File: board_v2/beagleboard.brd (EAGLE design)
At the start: 69.8 x 54.6 mm, 26 parts, among them U1 DWM1000, X1 5566-2, X2 04-JST-B4B-XH-A

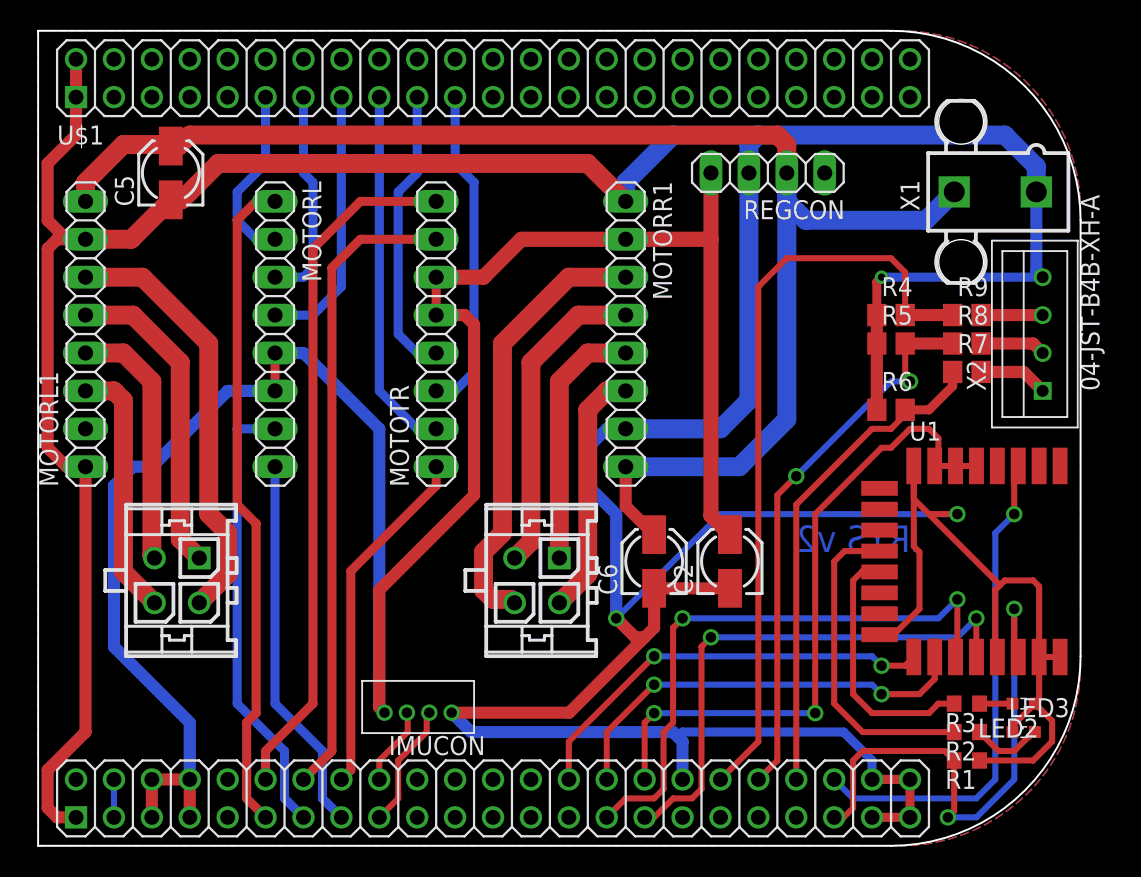
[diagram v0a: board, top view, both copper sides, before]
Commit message: added distance sensor connectors
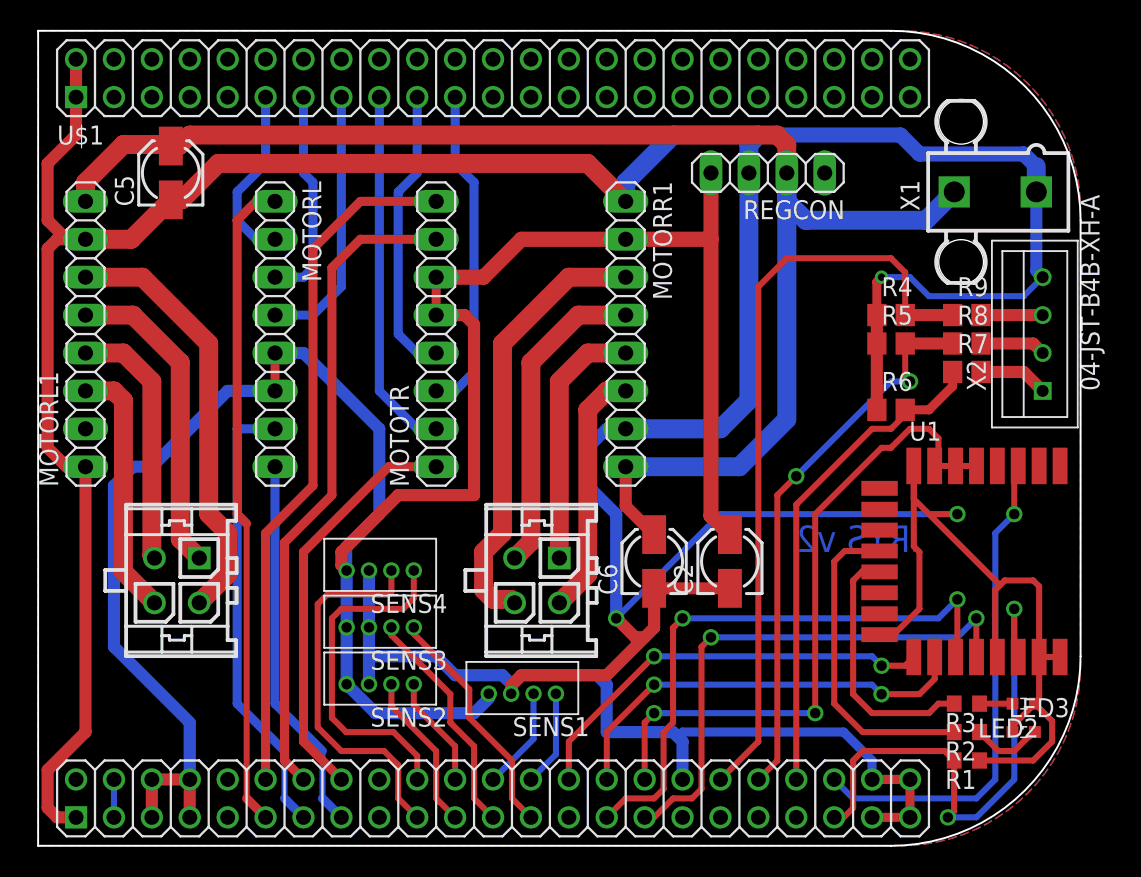
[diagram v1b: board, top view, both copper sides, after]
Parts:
- removed IMUCON: B4B-ZR, jst:B4B-ZR
- added SENS1, SENS2, SENS3, SENS4: B4B-ZR, jst:B4B-ZR
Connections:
- removed net N$100: U$1.71
- removed net N$74: U$1.66
- removed net N$75: U$1.68
- removed net N$76: U$1.70
- removed net N$77: U$1.72
- removed net N$97: U$1.65
- removed net N$98: U$1.67
- removed net N$99: U$1.69
- new net D1ECHO: SENS1.3, U$1.70
- new net D1TRIG: SENS1.4, U$1.72
- new net D2ECHO: SENS2.3, U$1.67
- new net D2TRIG: SENS2.4, U$1.68
- new net D3ECHO: SENS3.3, U$1.69
- new net D3TRIG: SENS3.4, U$1.71
- new net D4ECHO: SENS4.3, U$1.65
- new net D4TRIG: SENS4.4, U$1.66
- net +5V: now also SENS1.1, SENS2.1, SENS3.1, SENS4.1; no longer IMUCON.1
- net GND: now also SENS1.2, SENS2.2, SENS3.2, SENS4.2; no longer IMUCON.4
- net SCL1: no longer IMUCON.3
- net SDA1: no longer IMUCON.2
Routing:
- net D4ECHO: track 0.00 -> 25.4 mm
- net D4TRIG: track 0.00 -> 22.9 mm
- net D3TRIG: track 0.00 -> 16.0 mm
- net D3ECHO: track 0.00 -> 15.6 mm
- net GND: track 356.7 -> 371.9 mm
- net D2ECHO: track 0.00 -> 10.7 mm
- net SCL1: track 8.40 -> 0.00 mm
- net D2TRIG: track 0.00 -> 7.53 mm
- net D1ECHO: track 0.00 -> 6.87 mm
- net D1TRIG: track 0.00 -> 6.44 mm
- net SDA1: track 5.29 -> 0.00 mm
- net +5V: track 152.0 -> 156.4 mm
- net MREN: track 23.6 -> 27.5 mm
- net MRSTEP: track 42.9 -> 43.9 mm
- net MLEN: track 44.4 -> 43.9 mm

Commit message: gerbers
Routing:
- net +5V: track 156.4 -> 157.0 mm
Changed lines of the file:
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@@
 <board>
 <plain>
-<text x="61.595" y="20.32" size="1.778" layer="16" rot="MR0">iRYS v2</text>
+<text x="61.2775" y="19.685" size="1.778" layer="16" rot="MR0">iRYS v2</text>
 </plain>
 <attributes>
@@
 <wire x1="58.74" y1="29.845" x2="58.74" y2="38.42" width="0.6096" layer="1"/>
 <wire x1="58.74" y1="38.42" x2="59.055" y2="38.735" width="0.6096" layer="1"/>
-<via x="59.055" y="38.735" extent="1-16" drill="0.5" shape="octagon"/>
+<via x="59.055" y="38.735" extent="1-16" drill="0.5"/>
 <wire x1="43.18" y1="14.605" x2="42.545" y2="14.605" width="0.8128" layer="1"/>
 <wire x1="42.545" y1="14.605" x2="41.275" y2="15.875" width="0.8128" layer="1"/>
@@
 <wire x1="32.735" y1="10.825" x2="32.735" y2="10.51" width="0.8128" layer="16"/>
 <wire x1="32.735" y1="10.51" x2="31.75" y2="9.525" width="0.8128" layer="16"/>
-<wire x1="31.75" y1="9.525" x2="25.145" y2="9.525" width="0.8128" layer="16"/>
-<wire x1="25.145" y1="9.525" x2="23.21" y2="11.46" width="0.8128" layer="16"/>
+<wire x1="31.75" y1="9.525" x2="24.1925" y2="9.525" width="0.8128" layer="16"/>
 <wire x1="23.21" y1="19.08" x2="23.21" y2="15.27" width="0.8128" layer="16"/>
 <wire x1="23.21" y1="15.27" x2="23.21" y2="11.46" width="0.8128" layer="16"/>
+<wire x1="23.21" y1="11.46" x2="23.21" y2="10.5075" width="0.8128" layer="16"/>
+<wire x1="23.21" y1="10.5075" x2="24.1925" y2="9.525" width="0.8128" layer="16"/>
 </signal>
 <signal name="CSN">

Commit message: gpioadjustment
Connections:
- removed net N$105: U$1.81
- removed net N$106: U$1.83
- removed net N$107: U$1.85
- removed net N$45: U$1.7
- removed net N$46: U$1.9
- removed net N$69: U$1.56
- removed net N$92: U$1.55
- new net N$17: U$1.19
- new net N$19: U$1.21
- net +3V3: no longer U$1.78
- net D3TRIG: now also U$1.81; no longer U$1.71
- net D4ECHO: now also U$1.85; no longer U$1.65
- net D4TRIG: now also U$1.83; no longer U$1.66
- net MLM0: now also U$1.7; no longer U$1.11
- net MLM1: now also U$1.9; no longer U$1.13
- net MLM2: now also U$1.11; no longer U$1.15
- net MRM0: now also U$1.13; no longer U$1.17
- net MRM1: now also U$1.15; no longer U$1.21
- net MRM2: now also U$1.17; no longer U$1.19
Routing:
- net MRM0: track 24.5 -> 4.86 mm
- net MLM2: track 17.9 -> 5.23 mm
- net MLM1: track 14.5 -> 9.42 mm
- net MRM2: track 19.5 -> 14.4 mm
- net MLM0: track 12.1 -> 7.67 mm
- net MRM1: track 22.0 -> 17.6 mm
- net +3V3: track 44.5 -> 40.7 mm
- net D3TRIG: track 16.0 -> 14.2 mm
- net D4ECHO: track 25.4 -> 23.6 mm
- net D4TRIG: track 22.9 -> 21.3 mm
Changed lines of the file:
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@@
 <?xml version="1.0" encoding="utf-8"?>
 <!DOCTYPE eagle SYSTEM "eagle.dtd">
-<eagle version="7.1.0">
+<eagle version="7.7.0">
 <drawing>
 <settings>
@@
 <wire x1="65.415" y1="26.085" x2="64.015" y2="26.085" width="0.4064" layer="1"/>
 <wire x1="64.015" y1="26.085" x2="62.615" y2="26.085" width="0.4064" layer="1"/>
-<contactref element="U$1" pad="78"/>
-<wire x1="43.18" y1="5.08" x2="43.18" y2="8.89" width="0.4064" layer="1"/>
 <wire x1="43.18" y1="8.89" x2="43.815" y2="9.525" width="0.4064" layer="1"/>
 <via x="43.815" y="9.525" extent="1-16" drill="0.7"/>
@@
 <signal name="MRM0">
 <contactref element="MOTOTR" pad="2"/>
-<contactref element="U$1" pad="17"/>
-<wire x1="25.4" y1="50.8" x2="25.4" y2="31.115" width="0.6096" layer="16"/>
 <wire x1="25.4" y1="31.115" x2="27.94" y2="28.575" width="0.6096" layer="16"/>
 <wire x1="27.94" y1="28.575" x2="29.21" y2="28.575" width="0.6096" layer="16"/>
+<contactref element="U$1" pad="13"/>
+<wire x1="25.4" y1="31.115" x2="20.32" y2="50.8" width="0" layer="19" extent="16-16"/>
 </signal>
 <signal name="MRM1">
 <contactref element="MOTOTR" pad="3"/>
-<contactref element="U$1" pad="21"/>
-<wire x1="30.48" y1="50.8" x2="30.48" y2="46.355" width="0.6096" layer="16"/>
 <wire x1="30.48" y1="46.355" x2="31.75" y2="45.085" width="0.6096" layer="16"/>
 <wire x1="31.75" y1="45.085" x2="31.75" y2="32.385" width="0.6096" layer="16"/>
 <wire x1="31.75" y1="32.385" x2="30.48" y2="31.115" width="0.6096" layer="16"/>
 <wire x1="30.48" y1="31.115" x2="29.21" y2="31.115" width="0.6096" layer="16"/>
+<contactref element="U$1" pad="15"/>
+<wire x1="30.48" y1="46.355" x2="22.86" y2="50.8" width="0" layer="19" extent="16-16"/>
 </signal>
 <signal name="MRM2">
 <contactref element="MOTOTR" pad="4"/>
-<contactref element="U$1" pad="19"/>
-<wire x1="27.94" y1="50.8" x2="27.94" y2="45.72" width="0.6096" layer="16"/>
 <wire x1="27.94" y1="45.72" x2="26.67" y2="44.45" width="0.6096" layer="16"/>
 <wire x1="26.67" y1="44.45" x2="26.67" y2="34.925" width="0.6096" layer="16"/>
 <wire x1="26.67" y1="34.925" x2="27.94" y2="33.655" width="0.6096" layer="16"/>
 <wire x1="27.94" y1="33.655" x2="29.21" y2="33.655" width="0.6096" layer="16"/>
+<contactref element="U$1" pad="17"/>
+<wire x1="27.94" y1="45.72" x2="25.4" y2="50.8" width="0" layer="19" extent="16-16"/>
 </signal>
 <signal name="MLM0">
 <contactref element="MOTORL" pad="2"/>
-<contactref element="U$1" pad="11"/>
-<wire x1="17.78" y1="50.8" x2="17.78" y2="46.355" width="0.6096" layer="16"/>
 <wire x1="17.78" y1="46.355" x2="15.875" y2="44.45" width="0.6096" layer="16"/>
 <wire x1="15.875" y1="44.45" x2="15.875" y2="42.545" width="0.6096" layer="16"/>
 <wire x1="15.875" y1="42.545" x2="17.145" y2="41.275" width="0.6096" layer="16"/>
 <wire x1="17.145" y1="41.275" x2="18.415" y2="41.275" width="0.6096" layer="16"/>
+<contactref element="U$1" pad="7"/>
+<wire x1="17.78" y1="46.355" x2="12.7" y2="50.8" width="0" layer="19" extent="16-16"/>
 </signal>
 <signal name="MLM1">
 <contactref element="MOTORL" pad="3"/>
-<contactref element="U$1" pad="13"/>
-<wire x1="20.32" y1="50.8" x2="20.32" y2="45.72" width="0.6096" layer="16"/>
 <wire x1="20.32" y1="45.72" x2="20.955" y2="45.085" width="0.6096" layer="16"/>
 <wire x1="20.955" y1="45.085" x2="20.955" y2="39.37" width="0.6096" layer="16"/>
 <wire x1="20.955" y1="39.37" x2="20.32" y2="38.735" width="0.6096" layer="16"/>
 <wire x1="20.32" y1="38.735" x2="18.415" y2="38.735" width="0.6096" layer="16"/>
+<contactref element="U$1" pad="9"/>
+<wire x1="20.32" y1="45.72" x2="15.24" y2="50.8" width="0" layer="19" extent="16-16"/>
 </signal>
 <signal name="MLM2">
 <contactref element="MOTORL" pad="4"/>
-<contactref element="U$1" pad="15"/>
-<wire x1="22.86" y1="50.8" x2="22.86" y2="38.1" width="0.6096" layer="16"/>
 <wire x1="22.86" y1="38.1" x2="20.955" y2="36.195" width="0.6096" layer="16"/>
 <wire x1="20.955" y1="36.195" x2="18.415" y2="36.195" width="0.6096" layer="16"/>
+<contactref element="U$1" pad="11"/>
+<wire x1="22.86" y1="38.1" x2="17.78" y2="50.8" width="0" layer="19" extent="16-16"/>
 </signal>
 <signal name="N$18">
@@
 <contactref element="U$1" pad="5"/>
 </signal>
-<signal name="N$45">
-<contactref element="U$1" pad="7"/>
-</signal>
-<signal name="N$46">
-<contactref element="U$1" pad="9"/>
-</signal>
 <signal name="N$53">
 <contactref element="U$1" pad="23"/>
@@
 <contactref element="U$1" pad="45"/>
 </signal>
-<signal name="N$69">
-<contactref element="U$1" pad="56"/>
-</signal>
 <signal name="D4TRIG">
-<contactref element="U$1" pad="66"/>
 <contactref element="SENS4" pad="4"/>
 <wire x1="27.71" y1="19.08" x2="27.71" y2="17.2325" width="0.4064" layer="1"/>
@@
 <wire x1="22.86" y1="16.51" x2="22.225" y2="15.875" width="0.4064" layer="1"/>
 <wire x1="22.225" y1="15.875" x2="22.225" y2="9.2075" width="0.4064" layer="1"/>
-<wire x1="27.94" y1="5.08" x2="27.94" y2="6.6675" width="0.4064" layer="1"/>
 <wire x1="27.94" y1="6.6675" x2="26.3525" y2="8.255" width="0.4064" layer="1"/>
 <wire x1="26.3525" y1="8.255" x2="23.1775" y2="8.255" width="0.4064" layer="1"/>
 <wire x1="23.1775" y1="8.255" x2="22.225" y2="9.2075" width="0.4064" layer="1"/>
+<contactref element="U$1" pad="83"/>
+<wire x1="27.94" y1="6.6675" x2="50.8" y2="2.54" width="0" layer="19" extent="1-1"/>
 </signal>
 <signal name="D2TRIG">
@@
 <wire x1="37.235" y1="6.755" x2="35.56" y2="5.08" width="0.4064" layer="16"/>
 </signal>
-<signal name="N$92">
-<contactref element="U$1" pad="55"/>
-</signal>
 <signal name="D4ECHO">
-<contactref element="U$1" pad="65"/>
 <contactref element="SENS4" pad="3"/>
 <wire x1="26.21" y1="19.08" x2="26.21" y2="17.6375" width="0.4064" layer="1"/>
@@
 <wire x1="25.7175" y1="6.985" x2="26.67" y2="6.0325" width="0.4064" layer="1"/>
 <wire x1="26.67" y1="6.0325" x2="26.67" y2="3.81" width="0.4064" layer="1"/>
-<wire x1="26.67" y1="3.81" x2="27.94" y2="2.54" width="0.4064" layer="1"/>
+<contactref element="U$1" pad="85"/>
+<wire x1="26.67" y1="3.81" x2="53.34" y2="2.54" width="0" layer="19" extent="1-1"/>
 </signal>
 <signal name="D2ECHO">
@@
 <signal name="D3TRIG">
 <contactref element="SENS3" pad="4"/>
-<contactref element="U$1" pad="71"/>
 <wire x1="27.71" y1="15.27" x2="27.71" y2="14.835" width="0.4064" layer="1"/>
 <wire x1="27.71" y1="14.835" x2="31.4325" y2="11.1125" width="0.4064" layer="1"/>
@@
 <wire x1="31.4325" y1="9.2075" x2="34.29" y2="6.35" width="0.4064" layer="1"/>
 <wire x1="34.29" y1="6.35" x2="34.29" y2="3.81" width="0.4064" layer="1"/>
-<wire x1="34.29" y1="3.81" x2="35.56" y2="2.54" width="0.4064" layer="1"/>
+<contactref element="U$1" pad="81"/>
+<wire x1="34.29" y1="3.81" x2="48.26" y2="2.54" width="0" layer="19" extent="1-1"/>
 </signal>
 <signal name="D3ECHO">
@@
 <signal name="N$104">
 <contactref element="U$1" pad="79"/>
-</signal>
-<signal name="N$105">
-<contactref element="U$1" pad="81"/>
-</signal>
-<signal name="N$106">
-<contactref element="U$1" pad="83"/>
-</signal>
-<signal name="N$107">
-<contactref element="U$1" pad="85"/>
 </signal>
 <signal name="N$16">
@@
 <wire x1="7.62" y1="5.08" x2="7.62" y2="2.54" width="0.4064" layer="16"/>
 </signal>
+<signal name="N$17">
+<contactref element="U$1" pad="19"/>
+</signal>
+<signal name="N$19">
+<contactref element="U$1" pad="21"/>
+</signal>
 </signals>

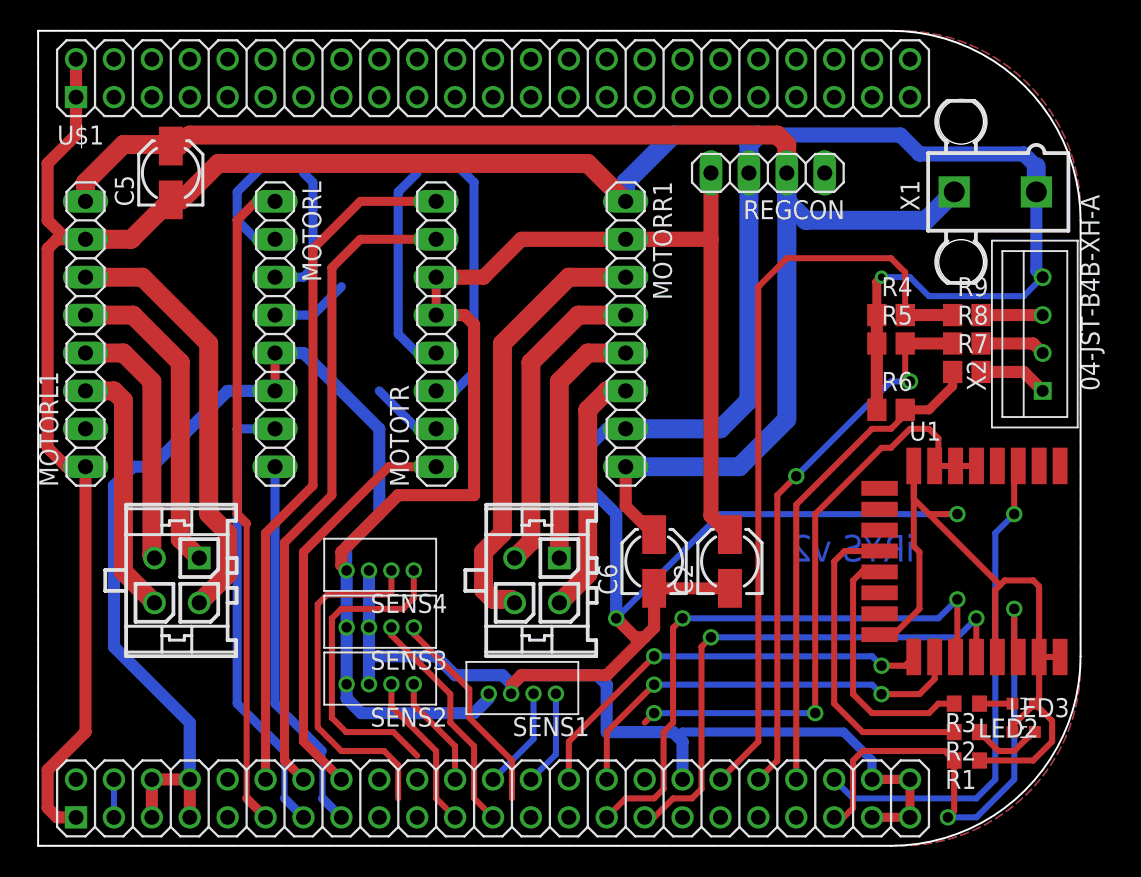
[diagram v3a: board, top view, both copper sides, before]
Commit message: check and reconfigure gpios
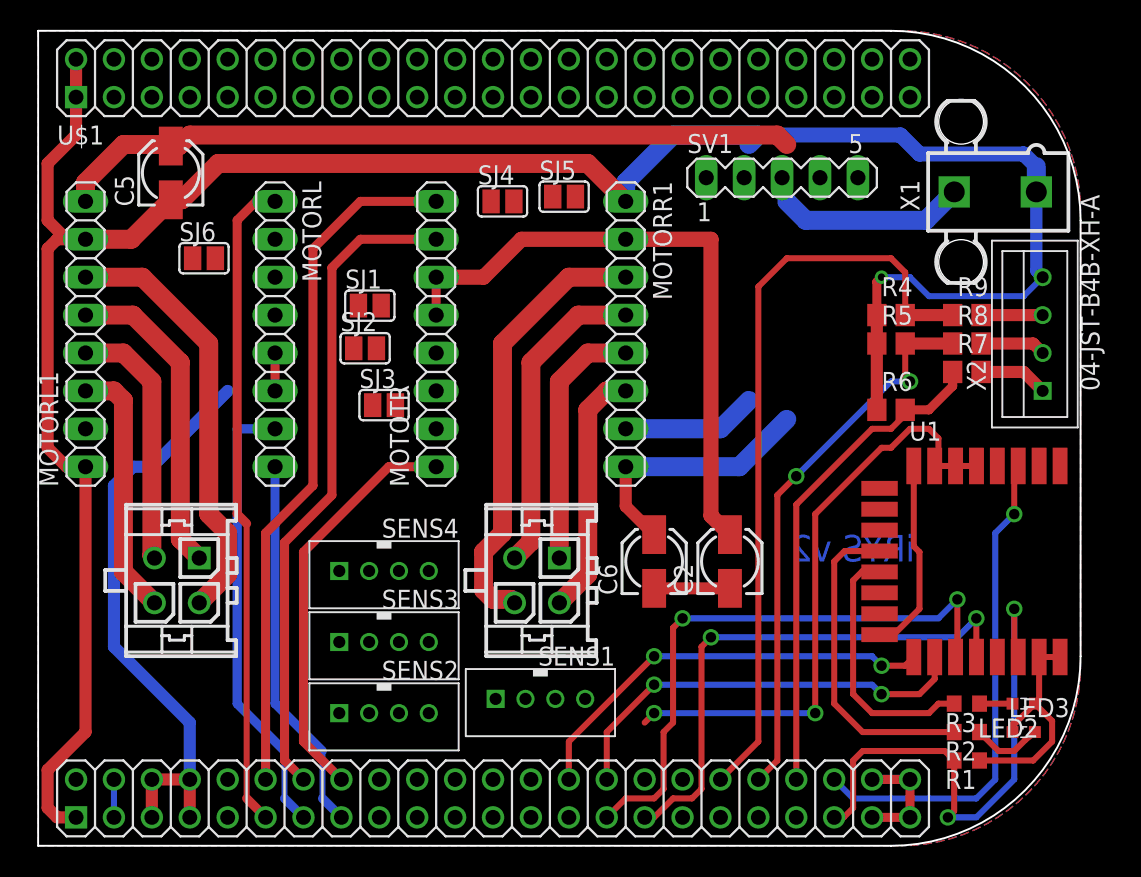
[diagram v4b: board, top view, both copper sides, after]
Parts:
- removed REGCON: (no value), pinhead:1X04
- added SJ1, SJ2, SJ3, SJ4, SJ5, SJ6: (no value), jumper:SJ
- added SV1: (no value), con-lstb:MA05-1
- SENS1, SENS2, SENS3, SENS4: value B4B-ZR -> 4PIN; device jst:B4B-ZR -> libsjst_eph:B4B-PH-K-S
- moved SENS4 3.72 mm to (25.7, 19.1)
- moved SENS2 3.55 mm to (25.7, 9.53)
- moved SENS3 3.51 mm to (25.7, 14.3)
- moved SENS1 2.71 mm to (36.2, 10.5)
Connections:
- removed net MLM0: MOTORL.2, U$1.7
- removed net MLM1: MOTORL.3, U$1.9
- removed net MLM2: MOTORL.4, U$1.11
- removed net MRM0: MOTOTR.2, U$1.13
- removed net MRM1: MOTOTR.3, U$1.15
- removed net MRM2: MOTOTR.4, U$1.17
- new net N$20: U$1.7
- new net N$42: U$1.9
- new net N$43: U$1.11
- new net N$44: U$1.13
- new net N$45: U$1.15
- new net N$46: U$1.17
- new net N$52: MOTORL.4, SJ3.1
- new net N$53: MOTORL.3, SJ2.1
- new net N$54: MOTORL.2, SJ1.1
- new net N$55: MOTOTR.2, SJ4.1
- new net N$65: MOTOTR.3, SJ5.1
- new net N$66: MOTOTR.4, SJ6.1
- net +12V: now also SV1.3; no longer REGCON.2
- net +5V: now also SJ1.2, SJ2.2, SJ3.2, SJ4.2, SJ5.2, SJ6.2, SV1.5; no longer REGCON.4
- net GND: now also SV1.4; no longer REGCON.3
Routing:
- net GND: track 371.9 -> 219.7 mm, vias 3 -> 1
- net +5V: track 157.0 -> 84.5 mm
- net D4ECHO: track 23.6 -> 0.00 mm
- net D4TRIG: track 21.3 -> 0.00 mm
- net +12V: track 100.2 -> 79.9 mm
- net MRM1: track 17.6 -> 0.00 mm
- net D3ECHO: track 15.6 -> 0.00 mm
- net MRM2: track 14.4 -> 0.00 mm
- net D3TRIG: track 14.2 -> 0.00 mm
- net D2ECHO: track 10.7 -> 0.00 mm
- net MLM1: track 9.42 -> 0.00 mm
- net MLM0: track 7.67 -> 0.00 mm
- net D2TRIG: track 7.53 -> 0.00 mm
- net D1ECHO: track 6.87 -> 0.00 mm
- net D1TRIG: track 6.44 -> 0.00 mm
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
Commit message: pin recinfiguration started
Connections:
- removed net SDA1: U$1.64
- new net N$67: U$1.81
- net D3TRIG: no longer U$1.81
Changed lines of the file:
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@@
 <signal name="D3TRIG">
 <contactref element="SENS3" pad="4"/>
-<contactref element="U$1" pad="81"/>
-<wire x1="28.7175" y1="14.2875" x2="48.26" y2="2.54" width="0" layer="19" extent="1-1"/>
 </signal>
 <signal name="D3ECHO">
@@
 <signal name="N$16">
 <contactref element="U$1" pad="48"/>
-</signal>
-<signal name="SDA1">
-<contactref element="U$1" pad="64"/>
 </signal>
 <signal name="SCL1">
@@
 <wire x1="12.8905" y1="40.005" x2="29.21" y2="33.655" width="0" layer="19" extent="1-1"/>
 </signal>
+<signal name="N$67">
+<contactref element="U$1" pad="81"/>
+</signal>
 </signals>
